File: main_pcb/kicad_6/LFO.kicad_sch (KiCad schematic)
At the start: 34 parts, among them J701 white_noise, Q701 2N3904, SW701 SW_SPDT_CO, U10 LF398_SOIC14, U6 TL072, U7 TL072

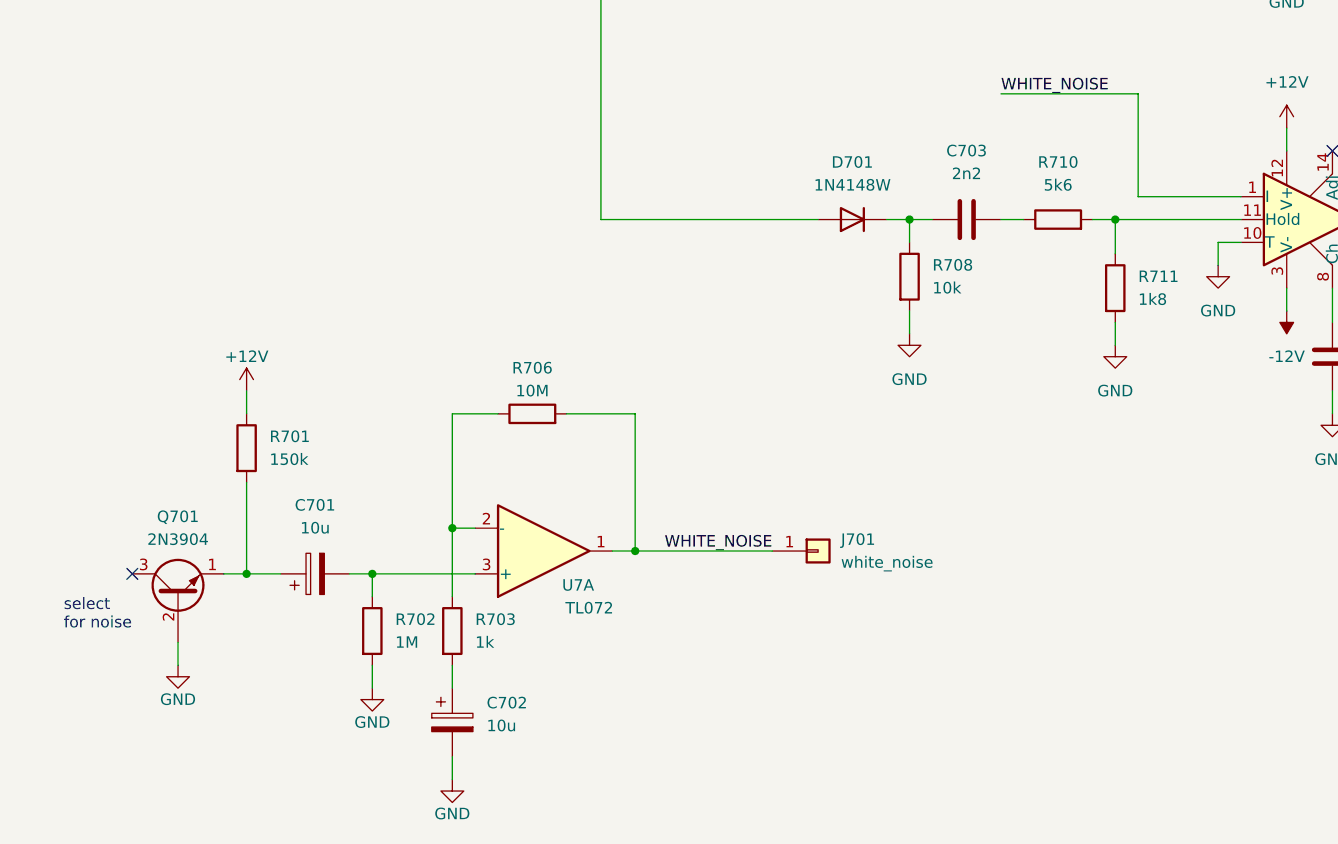
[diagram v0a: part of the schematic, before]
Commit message: Update rev 0.1, fix VCA tails, add local 2v5 regs, change some pot footprints
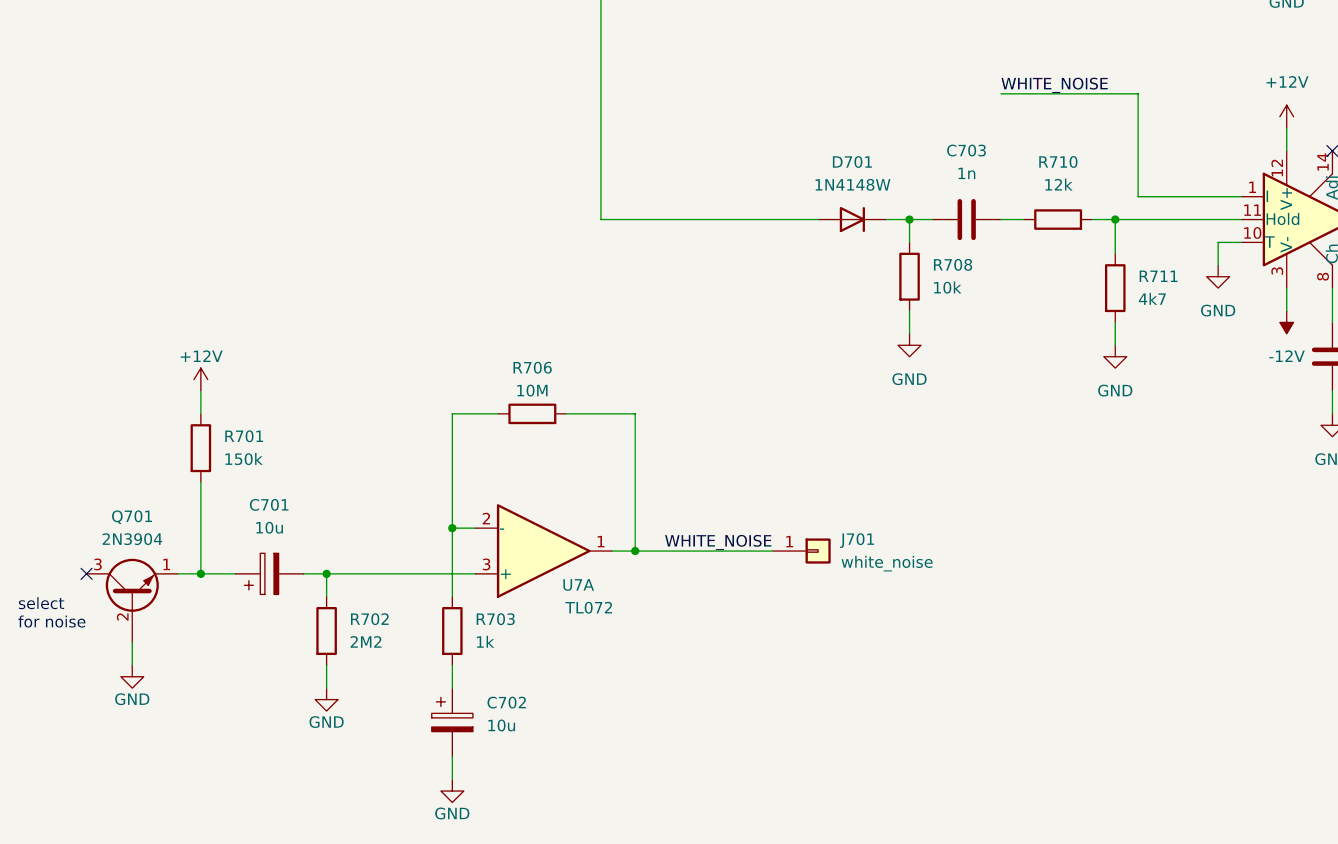
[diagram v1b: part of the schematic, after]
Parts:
- C703: value 2n2 -> 1n; footprint Capacitor_SMD:C_0805_2012Metric -> Capacitor_SMD:C_0603_1608Metric
- J701: now left out of the parts list
- R702: value 1M -> 2M2
- R710: value 5k6 -> 12k
- R711: value 1k8 -> 4k7
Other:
- moved on the sheet: C701, Q701, R701, R702

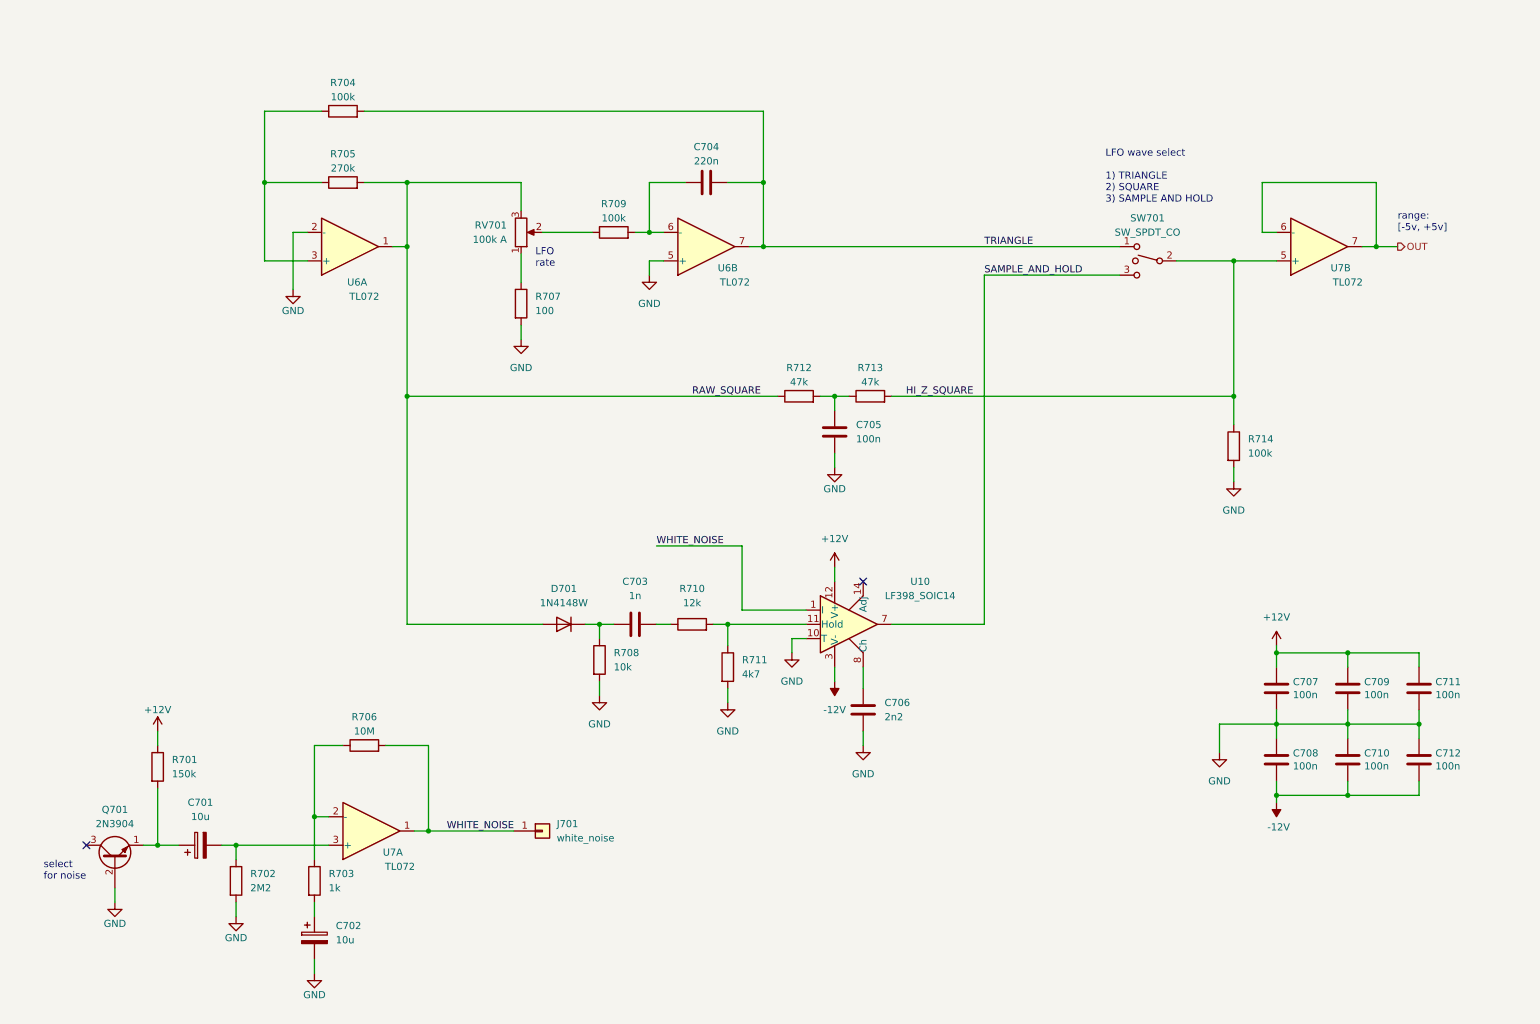
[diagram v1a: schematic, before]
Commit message: Add mod-wheel VCA, fix occasional VCO freq locking
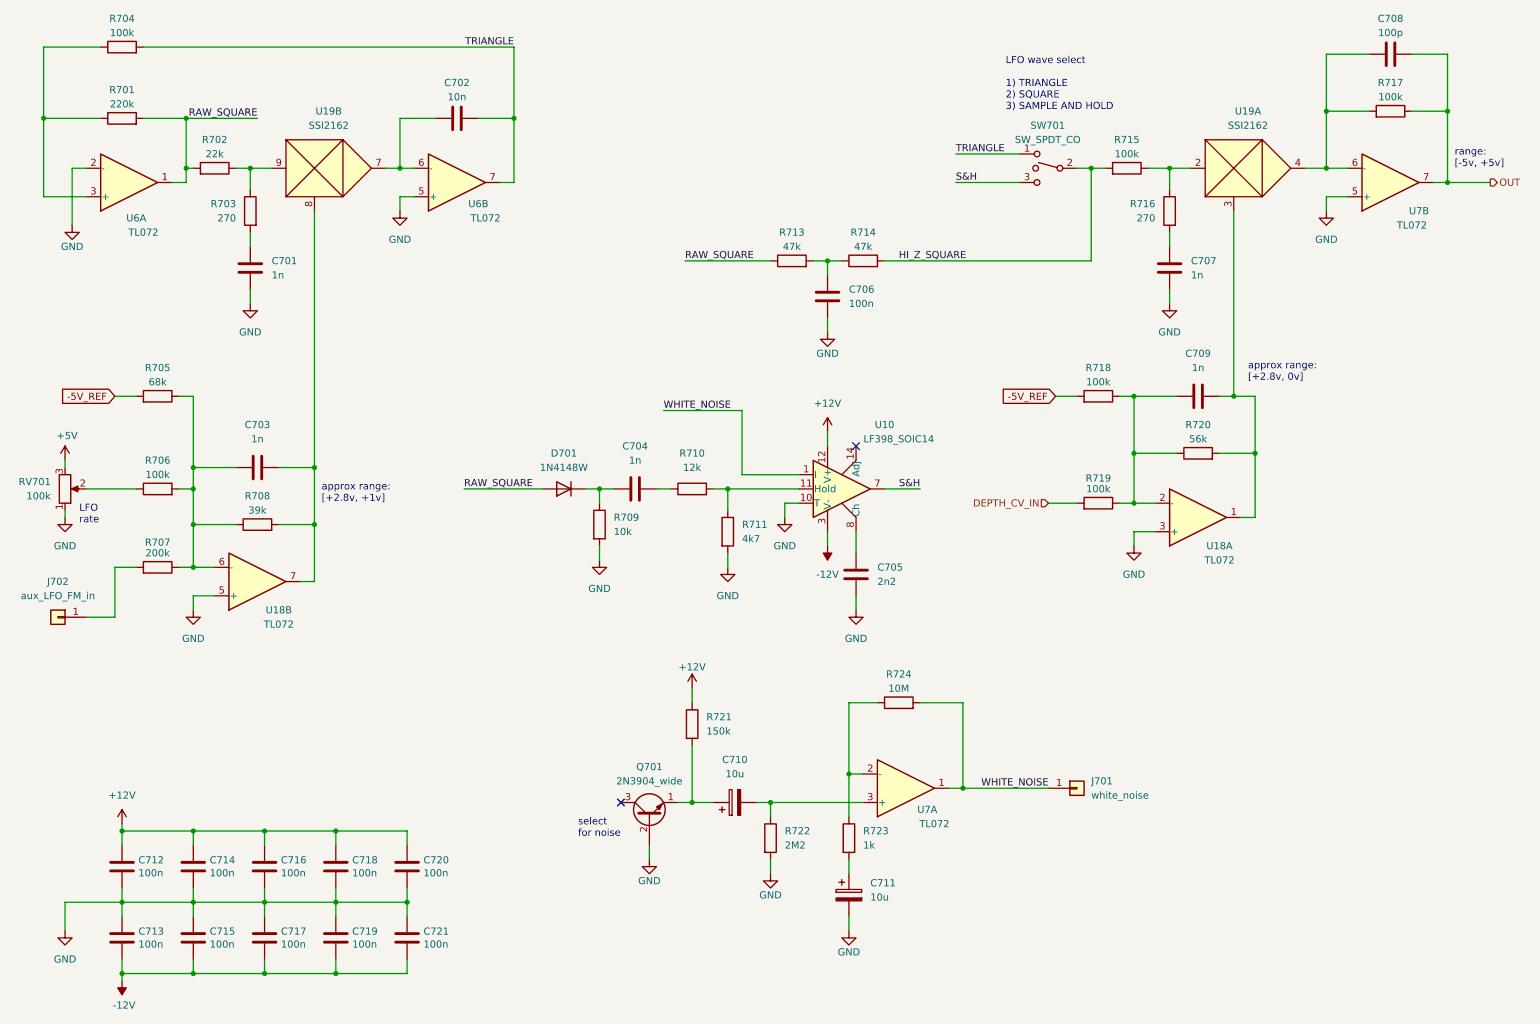
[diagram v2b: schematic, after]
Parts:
- removed Q701: 2N3904, Package_TO_SOT_THT:TO-92_Inline_Wide, symbol Transistor_BJT:2N3904
- removed R714: 100k, Resistor_SMD:R_0603_1608Metric, symbol Device:R
- added C701, C703, C707, C709: 1n, Capacitor_SMD:C_0603_1608Metric, symbol Device:C
- added C708: 100p, Capacitor_SMD:C_0603_1608Metric, symbol Device:C
- added C718, C719, C720, C721: 100n, Capacitor_SMD:C_0603_1608Metric, symbol Device:C
- added J702: aux_LFO_FM_in, TestPoint:TestPoint_Keystone_5000-5004_Miniature, symbol Connector_Generic:Conn_01x01
- added Q701: 2N3904_wide, Package_TO_SOT_THT:TO-92_Inline_Wide, symbol custom_symbols:2N3904_wide
- added R702: 22k, Resistor_SMD:R_0603_1608Metric, symbol Device:R
- added R703, R716: 270, Resistor_SMD:R_0603_1608Metric, symbol Device:R
- added R705: 68k, Resistor_SMD:R_0603_1608Metric, symbol Device:R
- added R708: 39k, Resistor_SMD:R_0603_1608Metric, symbol Device:R
- added R715, R717, R718, R719: 100k, Resistor_SMD:R_0603_1608Metric, symbol Device:R
- added R720: 56k, Resistor_SMD:R_0603_1608Metric, symbol Device:R
- added U18: TL072, Package_SO:SOIC-8_3.9x4.9mm_P1.27mm, symbol Amplifier_Operational:TL072
- added U19: SSI2162, Package_SO:SSOP-10_3.9x4.9mm_P1.00mm, symbol custom_symbols:SSI2162
- C702: renamed from C704; value 220n -> 10n; footprint Capacitor_THT:C_Rect_L7.0mm_W3.5mm_P5.00mm -> Capacitor_SMD:C_0805_2012Metric
- R701: renamed from R705; value 270k -> 220k
- R707: value 100 -> 200k
- RV701: value 100k A -> 100k
- renumbered C703 to C704, C706 to C705, C705 to C706, C701 to C710, C702 to C711, C707 to C712, C708 to C713, C709 to C714, C710 to C715, C711 to C716, C712 to C717, R709 to R706, R708 to R709, R712 to R713, R713 to R714, R701 to R721, R702 to R722, R703 to R723, R706 to R724
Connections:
- net +12V: now also C718.1, C720.1
- net -12V: now also C719.2, C721.2
- net GND: now also RV701.1, U7.5 (+), C701.2, C707.2, C718.2, C719.1, C720.2, C721.1, Q701.2 (B), U18.3 (+), U18.5 (+); no longer R707.2
- net HI_Z_SQUARE: now also R715.2; no longer U7.5 (+)
- net OUT: now also C708.1, R717.1; no longer U7.6 (-)
- net RAW_SQUARE: now also R702.2; no longer RV701.3
- net at C710.1, R721.2: now also Q701.1 (E)
- net at R707.1: now also R706.2, C703.2, R705.1, R708.1, U18.6 (-); no longer RV701.1
- net at C702.1, U6.6 (-): now also U19.7; no longer R706.2
- net SAMPLE_AND_HOLD renamed S&H
- new net: J702.1 (Pin_1), R707.2
- new net: C703.1, R708.2, U18.7, U19.8
- new net: C709.2, R718.1, R719.1, R720.1, U18.2 (-)
- new net: C709.1, R720.2, U18.1, U19.3
- new net: C708.2, R717.2, U19.4, U7.6 (-)
- new net: C707.1, R716.2
- new net: R715.1, R716.1, U19.2
- new net: R702.1, R703.1, U19.9
- new net: C701.1, R703.2
- new net +5V: RV701.3
- new net -5V_REF: R705.2, R718.2
- new net DEPTH_CV_IN: R719.2
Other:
- note added: "approx range: [+2.8v, +1v]"
- note added: "approx range: [+2.8v, 0v]"
- moved on the sheet: C702, C704, C705, C706, C710, C711, C712, C713, C714, C715, C716, C717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
